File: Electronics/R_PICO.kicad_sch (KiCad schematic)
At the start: 17 parts, among them J1 Battery_Connector, J10 MotorR, J2 VL53L0X, J3 VL53L0X, J4 VL53L0X, J5 VL53L0X, J6 KTIR0711S, J7 KTIR0711S, J8 TB6612FNG, J9 MotorL, U1 LM1117T-5.0

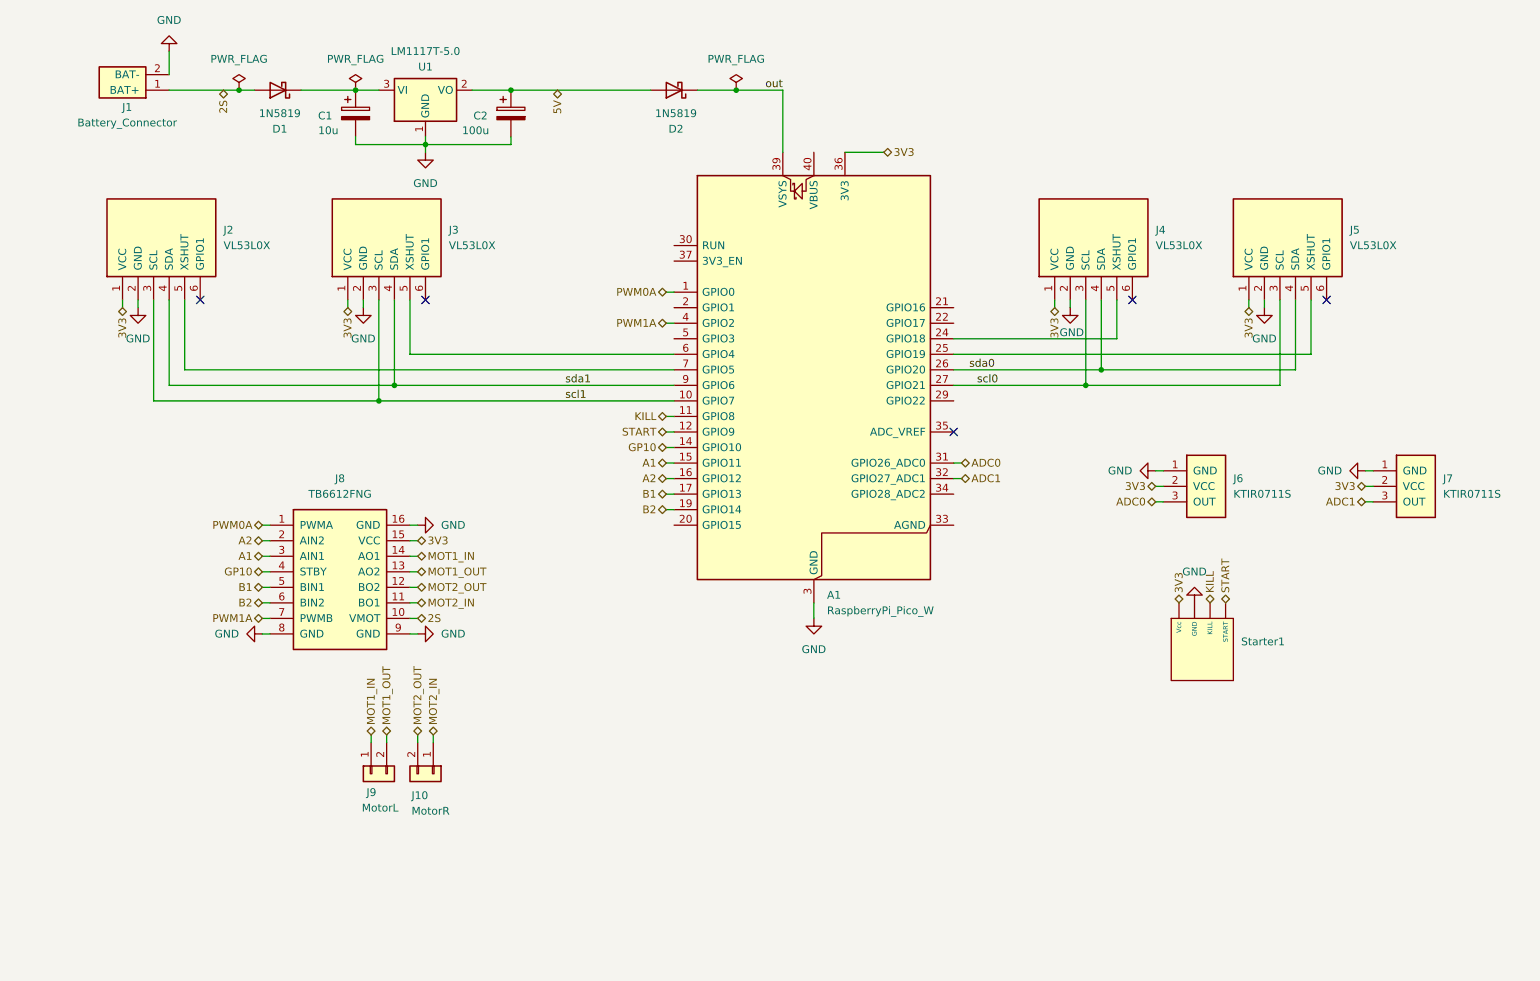
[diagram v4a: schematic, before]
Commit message: Feat: Finished PCB schematic, awaiting fabrication decision
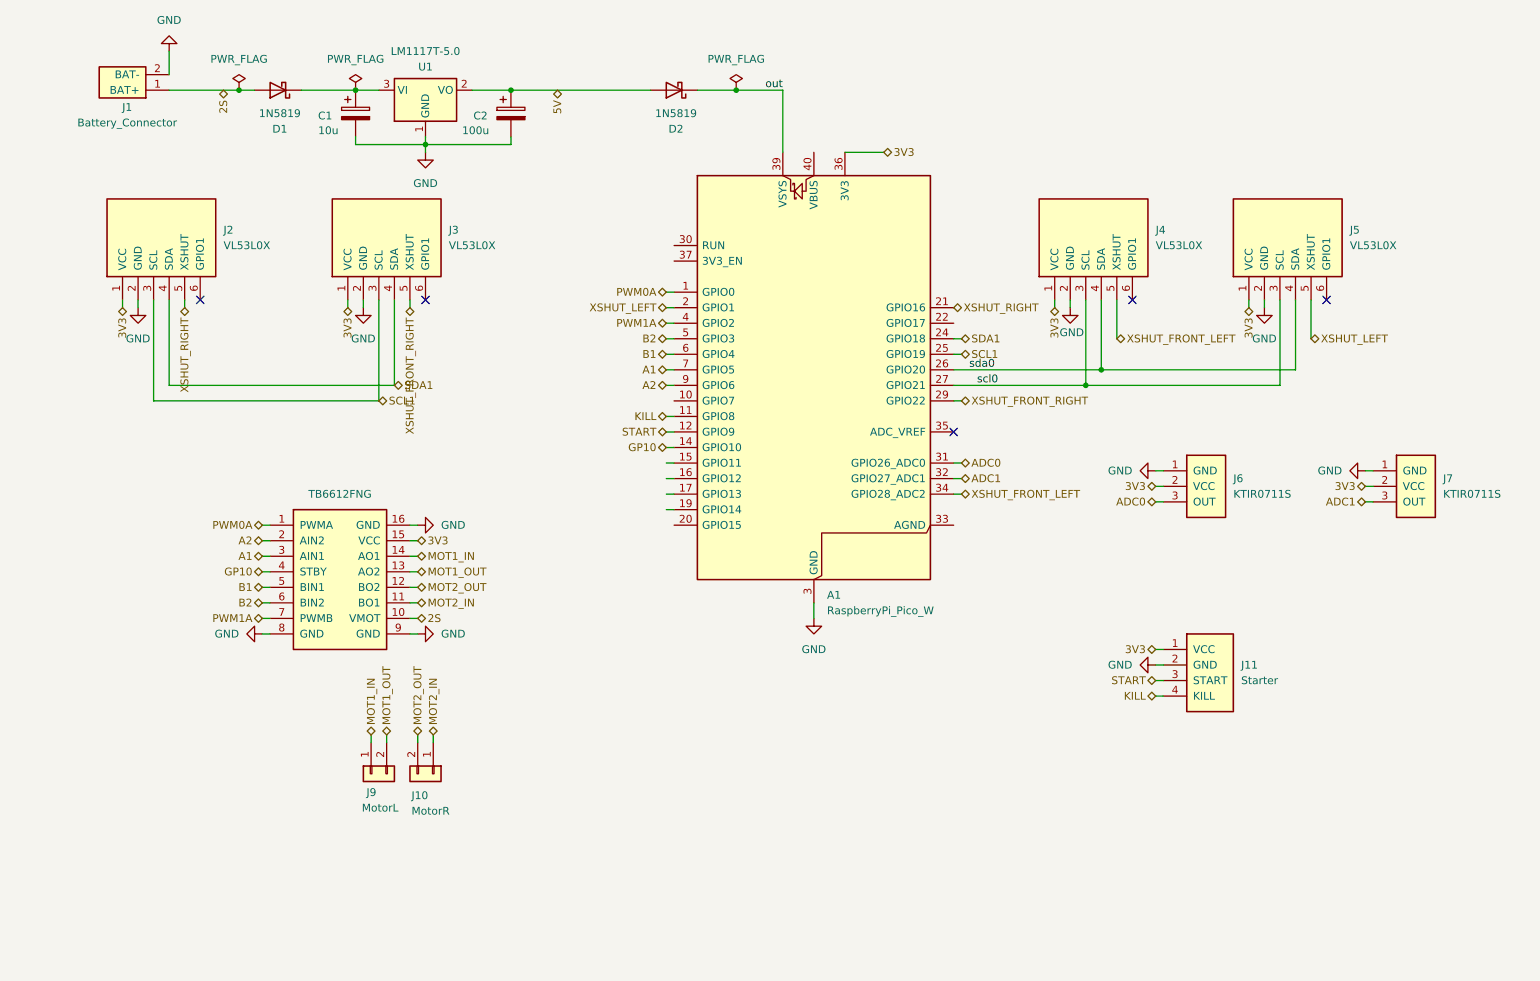
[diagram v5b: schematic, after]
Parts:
- removed Starter1: ~, Connector_PinHeader_2.54mm:PinHeader_1x04_P2.54mm_Vertical, symbol Own:Starter
- added J11: Starter, Connector_PinHeader_2.54mm:PinHeader_1x04_P2.54mm_Vertical, symbol ARENT_SYMBOLS_LIB:Starter
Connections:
- net 3V3: now also J11.1 (VCC)
- net A1: now also A1.7 (GPIO5); no longer A1.15 (GPIO11)
- net A2: now also A1.9 (GPIO6); no longer A1.16 (GPIO12)
- net B1: now also A1.6 (GPIO4); no longer A1.17 (GPIO13)
- net B2: now also A1.5 (GPIO3); no longer A1.19 (GPIO14)
- net GND: now also J11.2 (GND)
- net KILL: now also J11.4 (KILL)
- net START: now also J11.3 (START)
- net XSHUT_FRONT_RIGHT: now reaches J3.5 (XSHUT)
- net XSHUT_FRONT_RIGHT: now also A1.29 (GPIO22); no longer A1.6 (GPIO4)
- net SDA1: now reaches A1.24 (GPIO18)
- net SDA1: now also J2.4 (SDA), J3.4 (SDA); no longer J4.5 (XSHUT)
- net XSHUT_RIGHT: now reaches J2.5 (XSHUT)
- net XSHUT_RIGHT: now also A1.21 (GPIO16); no longer A1.7 (GPIO5)
- net SCL1: now reaches A1.25 (GPIO19)
- net SCL1: now also J2.3 (SCL), J3.3 (SCL); no longer J5.5 (XSHUT)
- net XSHUT_LEFT: now reaches A1.2 (GPIO1)
- net XSHUT_LEFT: now also J5.5 (XSHUT)
- net XSHUT_FRONT_LEFT: now reaches A1.34 (GPIO28_ADC2)
- net XSHUT_FRONT_LEFT: now also J4.5 (XSHUT)
- removed net scl1: A1.10 (GPIO7), J2.3 (SCL), J3.3 (SCL)
- removed net sda1: A1.9 (GPIO6), J2.4 (SDA), J3.4 (SDA)
